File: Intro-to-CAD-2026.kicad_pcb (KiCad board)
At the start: 4 copper layers, 100 x 100 mm, 260 parts, among them J1 ADC IN, J10 Conn_01x20_Socket, J11 SDR ANT, J12 SDR Out, J2 Conn_02x20_Counter_Clockwise, J3 Conn_02x20_Counter_Clockwise, J4 Conn_01x20_Socket, J5 Conn_01x02, J7 Conn_01x01_Pin, J8 BNC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

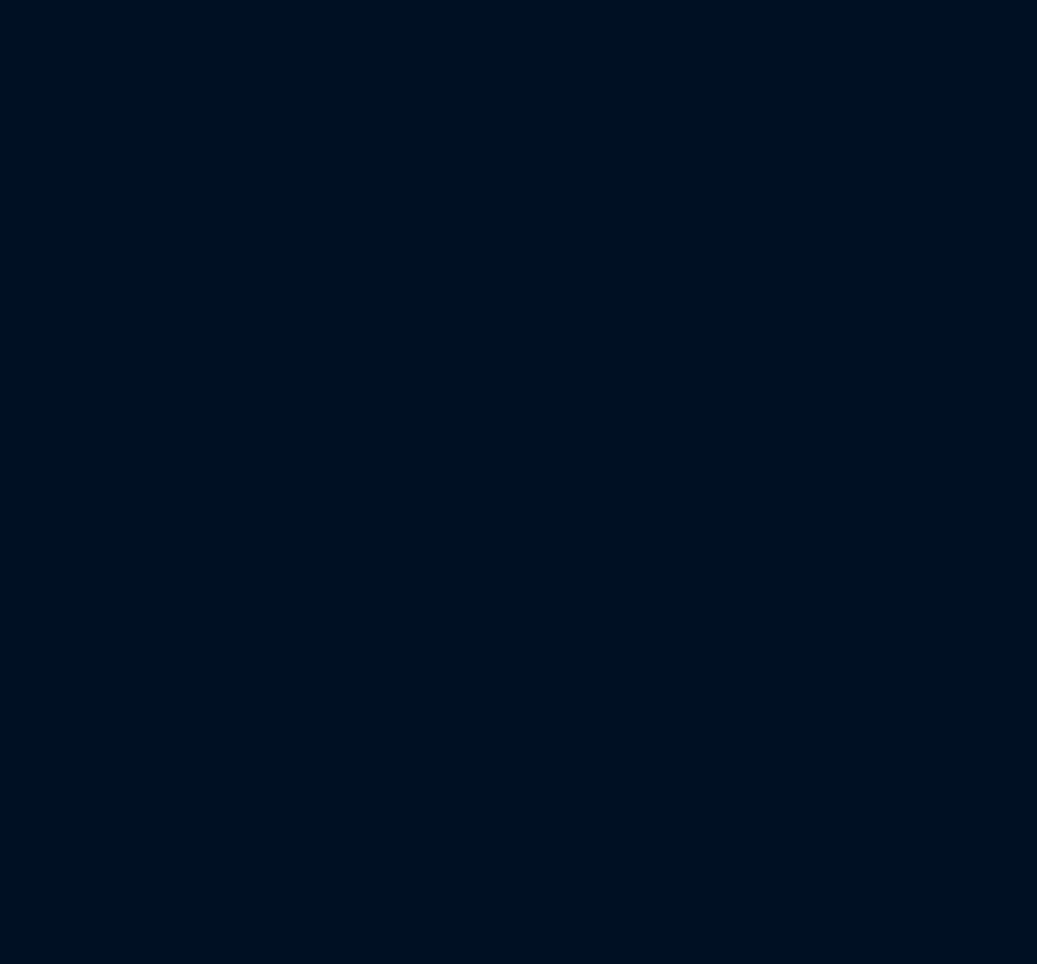
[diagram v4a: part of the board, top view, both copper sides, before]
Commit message: Imported Student Parts
Not using Project Instances yet.
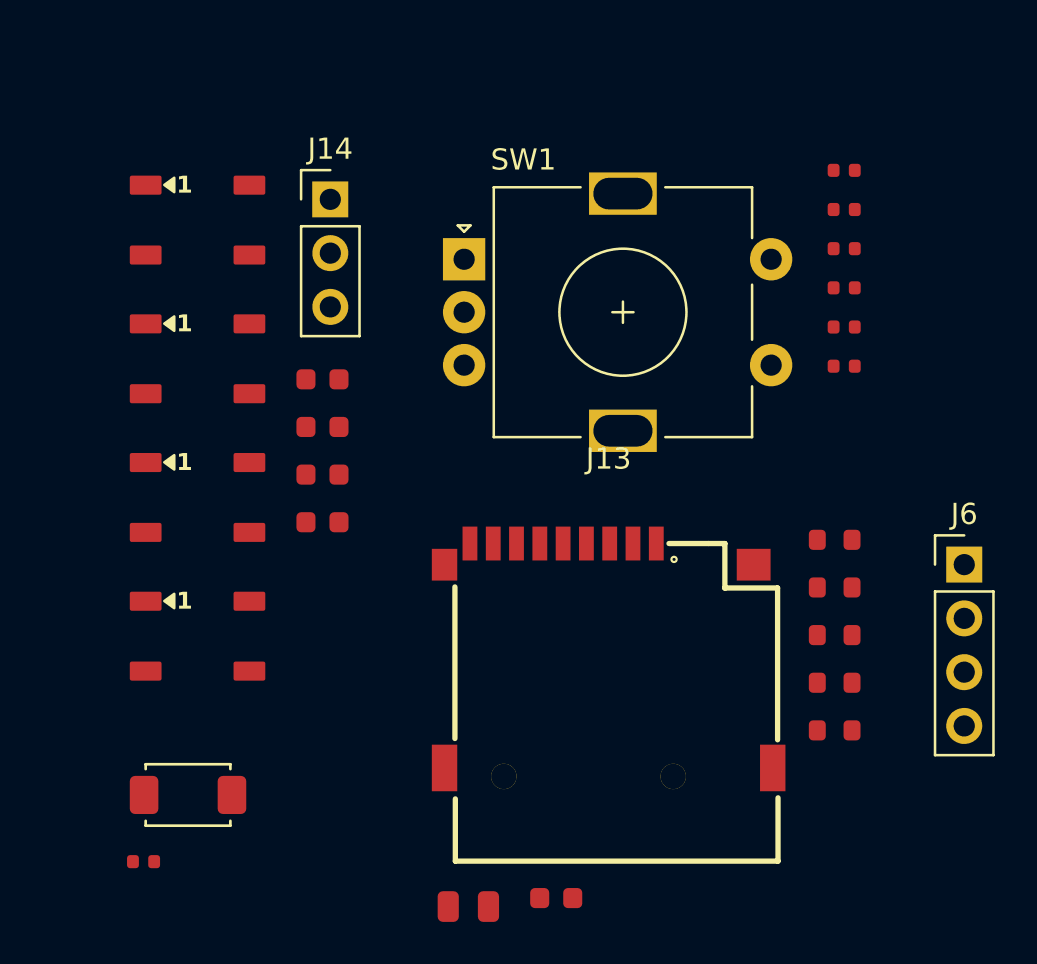
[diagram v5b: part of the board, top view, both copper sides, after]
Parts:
- added C62: 100nF, PCM_JLCPCB:C_0402, F.Cu at (318.3, 107.2)
- added C64: 10nF, PCM_JLCPCB:C_0402, F.Cu at (318.3, 109.1)
- added C65: 10nF, PCM_JLCPCB:C_0402, F.Cu at (318.3, 111.0)
- added C66: 10uF, PCM_JLCPCB:C_0805, F.Cu at (300.6, 142.0)
- added C67: 100nF, PCM_JLCPCB:C_0603, F.Cu at (304.7, 141.6)
- added C68: 100nF, PCM_JLCPCB:C_0603, F.Cu at (293.7, 117.1)
- added C69: 100nF, PCM_JLCPCB:C_0603, F.Cu at (293.7, 119.4)
- added C70: 100nF, PCM_JLCPCB:C_0603, F.Cu at (293.7, 121.6)
- added C71: 100nF, PCM_JLCPCB:C_0603, F.Cu at (293.7, 123.9)
- added D10: WS2812B, PCM_JLCPCB:LED_WS2812B_PLCC4_5.0x5.0mm_P3.2mm, F.Cu at (287.8, 122.7)
- added D11: WS2812B, PCM_JLCPCB:LED_WS2812B_PLCC4_5.0x5.0mm_P3.2mm, F.Cu at (287.8, 129.2)
- added D8: WS2812B, PCM_JLCPCB:LED_WS2812B_PLCC4_5.0x5.0mm_P3.2mm, F.Cu at (287.8, 109.6)
- added D9: WS2812B, PCM_JLCPCB:LED_WS2812B_PLCC4_5.0x5.0mm_P3.2mm, F.Cu at (287.8, 116.2)
- added J13: Micro_SD-TF_PUSH, 0_Personal:TF-SMD_TF-PUSH, F.Cu at (307.2, 130.2)
- added J14: Conn_01x03, Connector_PinHeader_2.54mm:PinHeader_1x03_P2.54mm_Vertical, F.Cu at (294.1, 108.6)
- added J6: HC-SR04 connector, Connector_PinHeader_2.54mm:PinHeader_1x04_P2.54mm_Vertical, F.Cu at (324.0, 125.9)
- added R57: 10kΩ, PCM_JLCPCB:R_0402, F.Cu at (318.3, 112.8)
- added R63: 10kΩ, PCM_JLCPCB:R_0402, F.Cu at (318.3, 114.7)
- added R64: 10kΩ, PCM_JLCPCB:R_0402, F.Cu at (318.3, 116.5)
- added R65: 10kΩ, PCM_JLCPCB:R_0603, F.Cu at (317.9, 124.7)
- added R66: 10kΩ, PCM_JLCPCB:R_0603, F.Cu at (317.9, 127.0)
- added R67: 10kΩ, PCM_JLCPCB:R_0603, F.Cu at (317.9, 129.2)
- added R68: 10kΩ, PCM_JLCPCB:R_0603, F.Cu at (317.9, 131.4)
- added R69: 10kΩ, PCM_JLCPCB:R_0603, F.Cu at (317.9, 133.7)
- added R70: 10kΩ, PCM_JLCPCB:R_0402, F.Cu at (285.2, 139.9)
- added S2: Tactile Button, 160gf, PCM_JLCPCB:SW_TS-1088-AR02016, F.Cu at (287.4, 136.8)
- added SW1: RotaryEncoder_Switch_MP, Rotary_Encoder:RotaryEncoder_Alps_EC11E-Switch_Vertical_H20mm, F.Cu at (300.4, 111.5)
